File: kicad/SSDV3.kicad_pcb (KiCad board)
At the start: 4 copper layers, 58.4 x 28.8 mm, 71 parts, among them J1 SolderPad, J2 SolderPad, J3 SolderPad, J4 SolderPad, J5 SolderPad, J6 SolderPad, J7 SolderPad_01x02, J8 SolderPad_1x03, Q1 CSD19537Q3, Q2 CSD19537Q3, Q3 BSZ096N10LS5, U1 LM5050-1, U2 LM5146RGYR

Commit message: Refactored schematic into A4 paper, updated PDFs
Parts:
- U2: value LM5146RGYR -> LM5146
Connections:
- net /BST renamed /buck_converter/BST
- net /COMP renamed /buck_converter/COMP
- net /COMP_RC1 renamed /buck_converter/COMP_RC1
- net /COMP_RC2 renamed /buck_converter/COMP_RC2
- net /FB renamed /buck_converter/FB
- net /HO renamed /buck_converter/HO
- net /ILIM renamed /buck_converter/ILIM
- net /JP_CFG1 renamed /buck_converter/JP_CFG1
- net /JP_CFG2 renamed /buck_converter/JP_CFG2
- net /LO renamed /buck_converter/LO
- net /RBST renamed /buck_converter/RBST
- net /RT renamed /buck_converter/RT
- net /SS_TRK renamed /buck_converter/SS_TRK
- net /SW renamed /buck_converter/SW
- net /SYNCIN renamed /buck_converter/SYNCIN
- net /U1_GATE renamed /rpp/U1_GATE
- net /U1_GND renamed /rpp/U1_GND
- net /U1_VS renamed /rpp/U1_VS
- net /U2_VIN renamed /buck_converter/U2_VIN
- net /VOUT_LED renamed /buck_converter/VOUT_LED
- net U1_EN renamed U2_EN
- NT1 pad 1: AGND -> PGND
- NT1 pad 2: PGND -> AGND

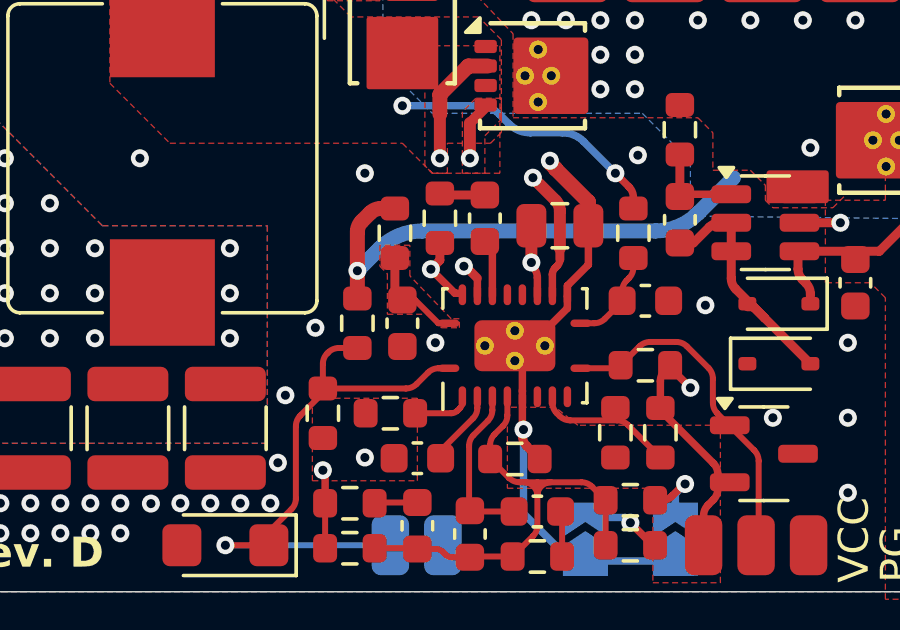
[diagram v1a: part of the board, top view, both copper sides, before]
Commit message: Layout tweaks, added copyright notice
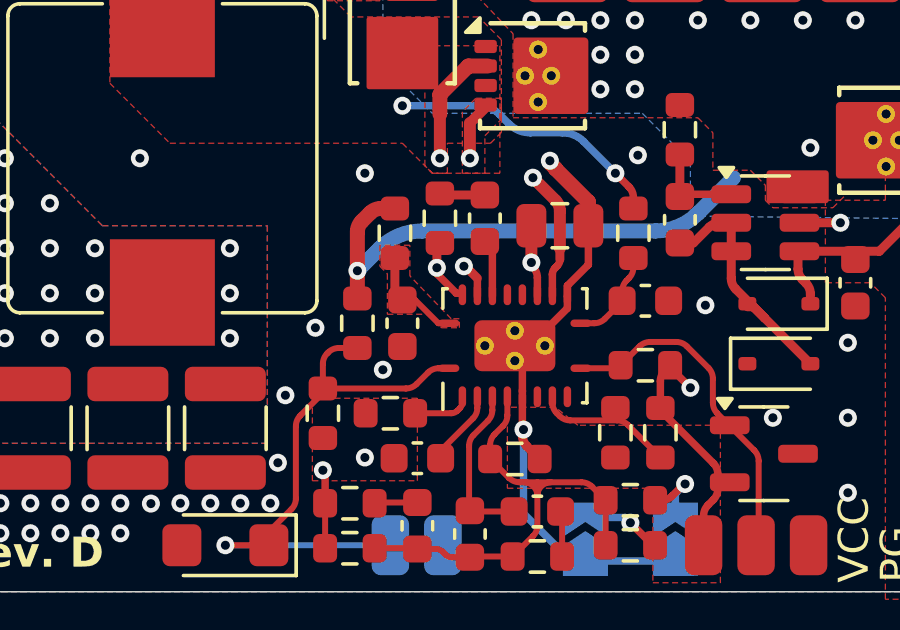
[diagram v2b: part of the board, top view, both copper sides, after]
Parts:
- turned NT1 to -90 degrees
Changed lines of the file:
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@@
 	(title_block
 		(title "Super Step Down V3")
-		(date "2025-11-03")
+		(date "2025-11-08")
 		(rev "D")
-		(company "Julian Joaquin")
-		(comment 1 "A 12S battery eliminator circuit (BEC) for UAS applications.")
+		(company "Author: Julian Joaquin")
+		(comment 1 "Licensed under CERN-OHL-W version 2")
+		(comment 2 "Copyright © Julian Joaquin, 2025")
+		(comment 4 "A 12S battery eliminator circuit (BEC) for UAS applications.")
 	)
 	(layers
@@
 	(footprint "NetTie:NetTie-2_SMD_Pad0.5mm"
 		(layer "F.Cu")
-		(at 154.65 121.625 90)
+		(at 154.65 121.625 -90)
 		(descr "Net tie, 2 pin, 0.5mm square SMD pads")
 		(tags "net tie")
@@
 		)
 		(property "Datasheet" "~"
-			(at 0 0 90)
+			(at 0 0 270)
 			(unlocked yes)
 			(layer "F.Fab")
@@
 		)
 		(property "Description" "Net tie, 2 pins"
-			(at 0 0 90)
+			(at 0 0 270)
 			(unlocked yes)
 			(layer "F.Fab")
@@
 		)
 		(property "LCSC ALT1" ""
-			(at 0 0 90)
+			(at 0 0 270)
 			(unlocked yes)
 			(layer "F.Fab")
@@
 		)
 		(property "PART ALT1" ""
-			(at 0 0 90)
+			(at 0 0 270)
 			(unlocked yes)
 			(layer "F.Fab")
@@
 		)
 		(property "ESR" ""
-			(at 0 0 90)
+			(at 0 0 270)
 			(unlocked yes)
 			(layer "F.Fab")
@@
 		)
 		(property "MANUFACTURER" ""
-			(at 0 0 90)
+			(at 0 0 270)
 			(unlocked yes)
 			(layer "F.Fab")
@@
 		)
 		(property "MAXIMUM_PACKAGE_HEIGHT" ""
-			(at 0 0 90)
+			(at 0 0 270)
 			(unlocked yes)
 			(layer "F.Fab")
@@
 		)
 		(property "Package" ""
-			(at 0 0 90)
+			(at 0 0 270)
 			(unlocked yes)
 			(layer "F.Fab")
@@
 		)
 		(property "Power" ""
-			(at 0 0 90)
+			(at 0 0 270)
 			(unlocked yes)
 			(layer "F.Fab")
@@
 		)
 		(property "STANDARD" ""
-			(at 0 0 90)
+			(at 0 0 270)
 			(unlocked yes)
 			(layer "F.Fab")
@@
 		)
 		(property "Voltage" ""
-			(at 0 0 90)
+			(at 0 0 270)
 			(unlocked yes)
 			(layer "F.Fab")
@@
 		)
 		(property "Part Number" ""
-			(at 0 0 90)
+			(at 0 0 270)
 			(unlocked yes)
 			(layer "F.Fab")
@@
 		)
 		(pad "1" smd circle
-			(at -0.5 0 90)
+			(at -0.5 0 270)
 			(size 0.25 0.25)
 			(layers "F.Cu")
@@
 		)
 		(pad "2" smd circle
-			(at 0.5 0 90)
+			(at 0.5 0 270)
 			(size 0.25 0.25)
 			(layers "F.Cu")
@@
 	)
 	(via
-		(at 151.75 120.5)
+		(at 150 121.4)
 		(size 0.6)
 		(drill 0.3)
@@
 	)
 	(segment
-		(start 152.4 118.85)
-		(end 151.6 118.05)
+		(start 151.8 118)
+		(end 151.8 117.275)
+		(width 0.3)
+		(layer "F.Cu")
+		(net 24)
+	)
+	(segment
+		(start 151.8 118)
+		(end 151.8 118.2)
 		(width 0.25)
 		(layer "F.Cu")
@@
 	)
 	(segment
-		(start 151.9 117.75)
-		(end 151.9 117.175)
-		(width 0.3)
+		(start 152.45 118.85)
+		(end 152.65 118.85)
+		(width 0.25)
 		(layer "F.Cu")
 		(net 24)
 	)
 	(segment
-		(start 151.6 118.05)
-		(end 151.9 117.75)
-		(width 0.3)
+		(start 151.8 117.275)
+		(end 151.9 117.175)
+		(width 0.25)
 		(layer "F.Cu")
 		(net 24)
@@
 	)
 	(segment
+		(start 151.8 118.2)
+		(end 152.45 118.85)
+		(width 0.25)
+		(layer "F.Cu")
+		(net 24)
+	)
+	(segment
 		(start 158.35 116.025)
 		(end 158.35 115.657107)
@@
 	)
 	(segment
-		(start 152.65 118.85)
-		(end 152.4 118.85)
-		(width 0.25)
-		(layer "F.Cu")
-		(net 24)
-	)
-	(segment
 		(start 151.9 112.875)
 		(end 151.9 112.225)
@@
 	)
 	(via
-		(at 151.6 118.05)
+		(at 151.8 118)
 		(size 0.6)
 		(drill 0.3)
@@
 	)
 	(segment
-		(start 151.9 117.75)
-		(end 151.9 114.35)
+		(start 151.8 118)
+		(end 151.9 117.9)
 		(width 0.5)
 		(layer "In2.Cu")
@@
 	)
 	(segment
-		(start 151.6 118.05)
-		(end 151.9 117.75)
+		(start 151.9 117.9)
+		(end 151.9 114.35)
 		(width 0.5)
 		(layer "In2.Cu")
